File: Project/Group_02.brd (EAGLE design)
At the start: 71.1 x 44.5 mm, 29 parts, among them J1 POWER_JACKPTH_LOCK, U1 +12v

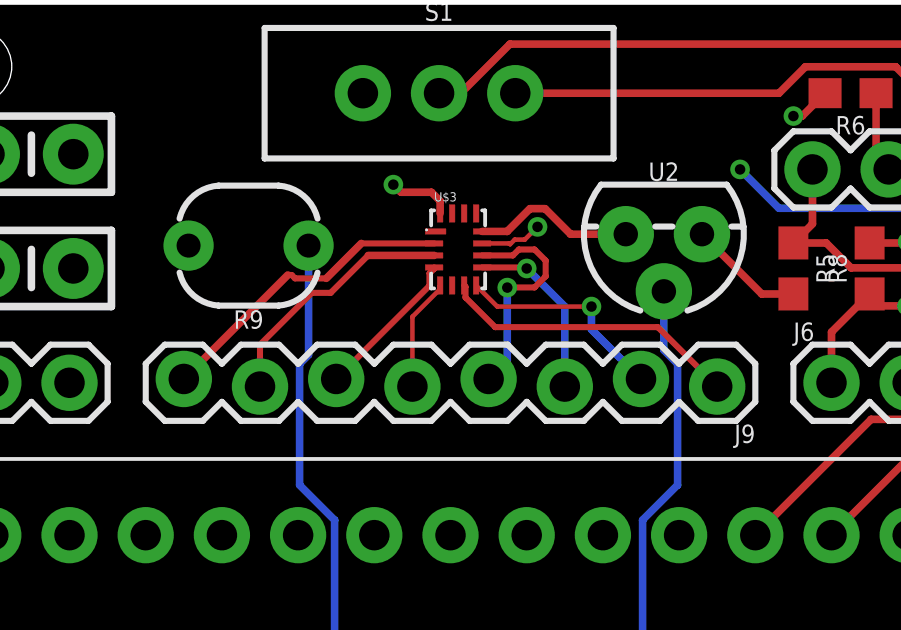
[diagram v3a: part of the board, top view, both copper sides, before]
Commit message: Ancora wire width 10 mils
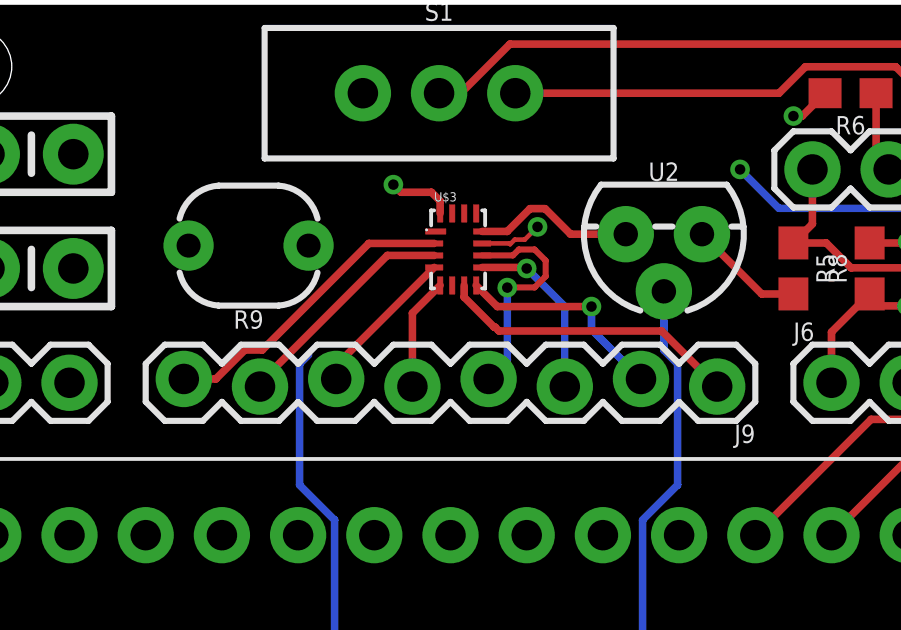
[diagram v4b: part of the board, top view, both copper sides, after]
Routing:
- net PHOTO_OUT: track 38.1 -> 34.5 mm
- net N$11: track 8.43 -> 7.69 mm
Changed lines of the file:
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@@
 <wire x1="24.169" y1="2.54" x2="24.13" y2="2.579" width="0.2032" layer="1"/>
 <wire x1="24.13" y1="2.579" x2="24.13" y2="6.35" width="0.254" layer="1"/>
-<wire x1="14.319" y1="36.322" x2="14.319" y2="32.6802125" width="0.254" layer="16"/>
 <wire x1="14.319" y1="32.6802125" x2="14.0208" y2="32.3820125" width="0.254" layer="16"/>
 <wire x1="15.1874" y1="15.2926" x2="24.13" y2="6.35" width="0.254" layer="16"/>
@@
 <wire x1="14.0208" y1="32.3820125" x2="14.0208" y2="28.34086875" width="0.254" layer="16"/>
 <wire x1="14.0208" y1="28.34086875" x2="15.1874" y2="27.17426875" width="0.254" layer="16"/>
+<wire x1="14.319" y1="32.6802125" x2="14.319" y2="36.322" width="0" layer="19" extent="16-16"/>
 </signal>
 <signal name="TEMP_OUT" class="1">
@@
 <contactref element="U$3" pad="2"/>
 <contactref element="J9" pad="8"/>
-<wire x1="18.504" y1="36.395" x2="16.075" y2="36.395" width="0.2032" layer="1"/>
-<wire x1="13.86659375" y1="35.2298" x2="13.753196875" y2="35.343196875" width="0.2032" layer="1"/>
-<wire x1="13.753196875" y1="35.343196875" x2="13.626196875" y2="35.343196875" width="0.2032" layer="1"/>
-<wire x1="13.626196875" y1="35.343196875" x2="10.16" y2="31.877" width="0.254" layer="1"/>
-<wire x1="16.075" y1="36.395" x2="14.9098" y2="35.2298" width="0.254" layer="1"/>
-<wire x1="14.9098" y1="35.2298" x2="13.86659375" y2="35.2298" width="0.2032" layer="1"/>
+<wire x1="18.504" y1="36.395" x2="16.329" y2="36.395" width="0.254" layer="1"/>
+<wire x1="12.7762" y1="32.8422" x2="12.1949875" y2="32.8422" width="0.254" layer="1"/>
+<wire x1="11.2297875" y1="31.877" x2="10.16" y2="31.877" width="0.254" layer="1"/>
+<wire x1="12.1949875" y1="32.8422" x2="11.2297875" y2="31.877" width="0.254" layer="1"/>
+<wire x1="16.329" y1="36.395" x2="12.7762" y2="32.8422" width="0.254" layer="1"/>
 </signal>
 <signal name="N$11">
 <contactref element="U$3" pad="3"/>
 <contactref element="J9" pad="7"/>
-<wire x1="12.7" y1="31.623" x2="12.7" y2="33.02" width="0.2032" layer="1"/>
-<wire x1="14.4272" y1="34.7472" x2="15.0571" y2="34.7472" width="0.2032" layer="1"/>
-<wire x1="16.3049" y1="35.995" x2="18.504" y2="35.995" width="0.254" layer="1"/>
-<wire x1="15.0571" y1="34.7472" x2="16.3049" y2="35.995" width="0.2032" layer="1"/>
-<wire x1="12.7" y1="33.02" x2="14.4272" y2="34.7472" width="0.2032" layer="1"/>
+<wire x1="18.504" y1="35.995" x2="16.945" y2="35.995" width="0.254" layer="1"/>
+<wire x1="12.7" y1="31.75" x2="12.7" y2="31.623" width="0.254" layer="1"/>
+<wire x1="16.945" y1="35.995" x2="12.7" y2="31.75" width="0.254" layer="1"/>
 </signal>
 <signal name="N$12">
 <contactref element="J9" pad="6"/>
 <contactref element="U$3" pad="4"/>
-<wire x1="15.24" y1="31.877" x2="18.35" y2="34.987" width="0.2032" layer="1"/>
-<wire x1="18.35" y1="34.987" x2="18.35" y2="35.39728125" width="0.2032" layer="1"/>
-<wire x1="18.504" y1="35.55128125" x2="18.504" y2="35.595" width="0.2032" layer="1"/>
-<wire x1="18.35" y1="35.39728125" x2="18.504" y2="35.55128125" width="0.2032" layer="1"/>
+<wire x1="18.504" y1="35.595" x2="15.24" y2="32.331" width="0.254" layer="1"/>
+<wire x1="15.24" y1="32.331" x2="15.24" y2="31.877" width="0.254" layer="1"/>
 </signal>
 <signal name="N$13">
 <contactref element="U$3" pad="5"/>
 <contactref element="J9" pad="5"/>
-<wire x1="17.78" y1="31.623" x2="17.78" y2="33.950025" width="0.1524" layer="1"/>
-<wire x1="17.78" y1="33.950025" x2="18.6802" y2="34.850225" width="0.1524" layer="1"/>
-<wire x1="18.6802" y1="34.850225" x2="18.6802" y2="34.9712" width="0.1524" layer="1"/>
-<wire x1="18.6802" y1="34.9712" x2="18.704" y2="34.995" width="0.1524" layer="1"/>
+<wire x1="18.704" y1="34.995" x2="17.78" y2="34.071" width="0.254" layer="1"/>
+<wire x1="17.78" y1="34.071" x2="17.78" y2="31.623" width="0.254" layer="1"/>
 </signal>
 <signal name="N$14">
@@
 <contactref element="U$3" pad="9"/>
 <contactref element="J9" pad="3"/>
-<wire x1="20.104" y1="35.595" x2="21.555" y2="35.595" width="0.2032" layer="1"/>
-<wire x1="21.555" y1="35.595" x2="21.59" y2="35.56" width="0.2032" layer="1"/>
+<wire x1="20.104" y1="35.595" x2="21.555" y2="35.595" width="0.254" layer="1"/>
+<wire x1="21.555" y1="35.595" x2="21.59" y2="35.56" width="0.254" layer="1"/>
 <via x="21.59" y="35.56" extent="1-16" drill="0.35"/>
 <wire x1="21.59" y1="35.56" x2="22.86" y2="34.29" width="0.254" layer="16"/>
@@
 <wire x1="23.749" y1="33.528" x2="23.749" y2="34.29" width="0.254" layer="16"/>
 <via x="23.749" y="34.29" extent="1-16" drill="0.35"/>
-<wire x1="23.749" y1="34.29" x2="20.609" y2="34.29" width="0.1524" layer="1"/>
-<wire x1="20.609" y1="34.29" x2="19.904" y2="34.995" width="0.1524" layer="1"/>
+<wire x1="20.609" y1="34.29" x2="23.749" y2="34.29" width="0.254" layer="1"/>
+<wire x1="19.904" y1="34.995" x2="20.609" y2="34.29" width="0.254" layer="1"/>
 </signal>
 <signal name="N$17">
 <contactref element="U$3" pad="7"/>
 <contactref element="J9" pad="1"/>
-<wire x1="27.94" y1="31.623" x2="25.9588" y2="33.6042" width="0.2032" layer="1"/>
-<wire x1="19.55" y1="34.59271875" x2="19.55" y2="34.949" width="0.2032" layer="1"/>
-<wire x1="19.55" y1="34.949" x2="19.504" y2="34.995" width="0.2032" layer="1"/>
-<wire x1="25.9588" y1="33.6042" x2="20.53851875" y2="33.6042" width="0.2032" layer="1"/>
-<wire x1="20.53851875" y1="33.6042" x2="19.55" y2="34.59271875" width="0.2032" layer="1"/>
+<wire x1="27.94" y1="31.623" x2="26.0858" y2="33.4772" width="0.254" layer="1"/>
+<wire x1="26.0858" y1="33.4772" x2="20.66551875" y2="33.4772" width="0.254" layer="1"/>
+<wire x1="20.53851875" y1="33.6042" x2="20.66551875" y2="33.4772" width="0.254" layer="1"/>
+<wire x1="20.5026" y1="33.6042" x2="20.53851875" y2="33.6042" width="0.254" layer="1"/>
+<wire x1="19.504" y1="34.995" x2="19.504" y2="34.6028" width="0.254" layer="1"/>
+<wire x1="19.504" y1="34.6028" x2="20.5026" y2="33.6042" width="0.254" layer="1"/>
 </signal>
 <signal name="MUX_OUT/1.4C">

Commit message: Pulizia cavi
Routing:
- net PHOTO_OUT: track 34.5 -> 38.1 mm
- net I2C_A1: track 11.3 -> 10.5 mm
- net I2C_SCL_2: track 11.5 -> 10.7 mm
- net I2C_SCL_1: track 12.0 -> 11.3 mm
- net I2C_SDA_1: track 12.2 -> 11.5 mm
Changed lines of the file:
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@@
 <wire x1="37.74" y1="29.993" x2="37.465" y2="29.718" width="0.254" layer="1"/>
 <via x="37.465" y="29.718" extent="1-16" drill="0.35"/>
-<wire x1="49.149" y1="31.281" x2="48.514" y2="34.5442" width="0" layer="19" extent="1-1"/>
-<wire x1="37.74" y1="30.745" x2="45.72" y2="31.281" width="0" layer="19" extent="1-1"/>
-<wire x1="38.1" y1="36.322" x2="37.74" y2="30.745" width="0" layer="19" extent="1-1"/>
-<wire x1="35.56" y1="36.41" x2="38.1" y2="36.322" width="0" layer="19" extent="1-1"/>
-<wire x1="30.48" y1="34.71" x2="33.02" y2="36.41" width="0" layer="19" extent="1-1"/>
-<wire x1="30.48" y1="40.64" x2="33.02" y2="36.41" width="0" layer="19" extent="1-1"/>
-<wire x1="21.9506" y1="36.9467375" x2="27.432" y2="36.703" width="0" layer="19" extent="1-1"/>
-<wire x1="18.704" y1="37.395" x2="20.104" y2="36.395" width="0" layer="19" extent="1-1"/>
-<wire x1="10.319" y1="36.322" x2="17.145" y2="38.354" width="0" layer="19" extent="1-1"/>
-<wire x1="6.477" y1="35.56" x2="10.319" y2="36.322" width="0" layer="19" extent="1-1"/>
-<wire x1="6.477" y1="39.37" x2="6.477" y2="35.56" width="0" layer="19" extent="1-1"/>
-<wire x1="6.35" y1="31.75" x2="6.477" y2="35.56" width="0" layer="19" extent="1-1"/>
-<wire x1="3.81" y1="26.67" x2="6.35" y2="31.75" width="0" layer="19" extent="1-1"/>
-<wire x1="67.31" y1="6.35" x2="53.975" y2="30.353" width="0" layer="19" extent="1-1"/>
 </signal>
 <signal name="GND">
@@
 <wire x1="21.69925" y1="37.5535375" x2="20.9407125" y2="36.795" width="0.254" layer="1"/>
 <wire x1="20.9407125" y1="36.795" x2="20.104" y2="36.795" width="0.254" layer="1"/>
-<wire x1="62.912" y1="34.1884" x2="58.769" y2="37.9246" width="0" layer="19" extent="1-1"/>
-<wire x1="45.426" y1="39.878" x2="58.769" y2="37.9246" width="0" layer="19" extent="1-1"/>
-<wire x1="43.54" y1="35.295" x2="45.426" y2="39.878" width="0" layer="19" extent="1-1"/>
-<wire x1="43.54" y1="32.045" x2="43.54" y2="35.295" width="0" layer="19" extent="1-1"/>
-<wire x1="38.1" y1="38.851" x2="43.54" y2="35.295" width="0" layer="19" extent="1-1"/>
-<wire x1="24.892" y1="36.703" x2="28.702" y2="38.862" width="0" layer="19" extent="1-1"/>
-<wire x1="3.683" y1="35.56" x2="20.104" y2="36.795" width="0" layer="19" extent="1-1"/>
-<wire x1="3.683" y1="39.37" x2="3.683" y2="35.56" width="0" layer="19" extent="1-1"/>
-<wire x1="3.81" y1="31.75" x2="3.683" y2="35.56" width="0" layer="19" extent="1-1"/>
-<wire x1="6.35" y1="26.67" x2="3.81" y2="31.75" width="0" layer="19" extent="1-1"/>
-<wire x1="19.05" y1="2.54" x2="6.35" y2="26.67" width="0" layer="19" extent="1-1"/>
-<wire x1="25.869" y1="2.54" x2="19.05" y2="2.54" width="0" layer="19" extent="1-1"/>
-<wire x1="64.77" y1="6.35" x2="62.912" y2="34.1884" width="0" layer="19" extent="1-1"/>
 </signal>
 <signal name="12V">
@@
 <wire x1="14.0208" y1="32.3820125" x2="14.0208" y2="28.34086875" width="0.254" layer="16"/>
 <wire x1="14.0208" y1="28.34086875" x2="15.1874" y2="27.17426875" width="0.254" layer="16"/>
-<wire x1="14.319" y1="32.6802125" x2="14.319" y2="36.322" width="0" layer="19" extent="16-16"/>
+<wire x1="14.319" y1="36.322" x2="14.319" y2="32.6802125" width="0.254" layer="16"/>
 </signal>
 <signal name="TEMP_OUT" class="1">
@@
 <contactref element="U$2" pad="10"/>
 <contactref element="R5" pad="1"/>
-<wire x1="37.74" y1="34.645" x2="37.696" y2="34.689" width="0.254" layer="1"/>
-<wire x1="37.696" y1="34.689" x2="37.01838125" y2="34.689" width="0.254" layer="1"/>
 <wire x1="31.115" y1="38.862" x2="31.115" y2="37.045" width="0.254" layer="1"/>
 <wire x1="31.115" y1="37.045" x2="30.48" y2="36.41" width="0.254" layer="1"/>
@@
 <wire x1="45.47386875" y1="34.6938" x2="45.8442" y2="34.32346875" width="0.254" layer="1"/>
 <wire x1="45.8442" y1="34.32346875" x2="45.8442" y2="33.79973125" width="0.254" layer="1"/>
-<wire x1="43.54" y1="33.995" x2="44.25133125" y2="33.995" width="0.254" layer="1"/>
 <wire x1="45.8442" y1="33.79973125" x2="45.7395" y2="33.69503125" width="0.254" layer="1"/>
 <wire x1="45.7395" y1="33.69503125" x2="45.7395" y2="33.0005" width="0.254" layer="1"/>
@@
 <wire x1="51.435" y1="39.243" x2="48.983" y2="36.791" width="0.254" layer="1"/>
 <wire x1="48.983" y1="36.791" x2="48.983" y2="35.56" width="0.254" layer="1"/>
-<wire x1="44.26161875" y1="34.689" x2="43.584" y2="34.689" width="0.254" layer="1"/>
-<wire x1="43.584" y1="34.689" x2="43.54" y2="34.645" width="0.254" layer="1"/>
 <wire x1="48.983" y1="35.56" x2="48.8192125" y2="35.56" width="0.254" layer="1"/>
 <wire x1="48.8192125" y1="35.56" x2="47.9382125" y2="36.441" width="0.254" layer="1"/>
@@
 <contactref element="R2" pad="1"/>
 <wire x1="43.54" y1="32.695" x2="44.45" y2="32.695" width="0.254" layer="1"/>
-<wire x1="44.56086875" y1="32.695" x2="44.5967875" y2="32.695" width="0.254" layer="1"/>
 <wire x1="49.149" y1="32.981" x2="51.015" y2="31.115" width="0.254" layer="1"/>
 <wire x1="51.015" y1="31.115" x2="51.562" y2="31.115" width="0.254" layer="1"/>
@@
 <contactref element="U$1" pad="51"/>
 <contactref element="D1" pad="A"/>
-<wire x1="6.35" y1="6.35" x2="6.35" y2="2.77" width="0.254" layer="1"/>
-<wire x1="6.35" y1="2.77" x2="6.12" y2="2.54" width="0.2032" layer="1"/>
+<wire x1="6.35" y1="2.77" x2="6.35" y2="6.35" width="0.254" layer="1"/>
+<wire x1="6.12" y1="2.54" x2="6.35" y2="2.77" width="0.254" layer="1"/>
 </signal>
 <signal name="N$9">
@@
 <contactref element="U$2" pad="2"/>
 <contactref element="U$1" pad="7"/>
-<wire x1="43.54" y1="31.395" x2="43.584" y2="31.351" width="0.254" layer="1"/>
-<wire x1="43.584" y1="31.351" x2="44.26161875" y2="31.351" width="0.254" layer="1"/>
 <wire x1="49.53" y1="29.21" x2="52.07" y2="26.67" width="0.254" layer="1"/>
-<wire x1="46.3817875" y1="29.21" x2="49.53" y2="29.21" width="0.254" layer="1"/>
-<wire x1="46.3817875" y1="29.23083125" x2="46.3817875" y2="29.21" width="0.254" layer="1"/>
-<wire x1="44.9406" y1="30.61526875" x2="45.10426875" y2="30.4516" width="0.254" layer="1"/>
-<wire x1="45.10426875" y1="30.4516" x2="45.1401875" y2="30.4516" width="0.254" layer="1"/>
-<wire x1="45.1401875" y1="30.4516" x2="46.3817875" y2="29.21" width="0.254" layer="1"/>
-<wire x1="43.54" y1="31.395" x2="44.25354375" y2="31.395" width="0.254" layer="1"/>
-<wire x1="44.25354375" y1="31.395" x2="44.9406" y2="30.70794375" width="0.254" layer="1"/>
-<wire x1="44.9406" y1="30.70794375" x2="44.9406" y2="30.61526875" width="0.254" layer="1"/>
+<wire x1="44.762934375" y1="30.792934375" x2="46.34586875" y2="29.21" width="0.254" layer="1"/>
+<wire x1="46.34586875" y1="29.21" x2="49.53" y2="29.21" width="0.254" layer="1"/>
+<wire x1="44.5694" y1="31.07914375" x2="44.39914375" y2="31.2494" width="0.254" layer="1"/>
+<wire x1="44.39914375" y1="31.2494" x2="43.6856" y2="31.2494" width="0.254" layer="1"/>
+<wire x1="43.6856" y1="31.2494" x2="43.54" y2="31.395" width="0.254" layer="1"/>
+<wire x1="44.762934375" y1="30.792934375" x2="44.5694" y2="30.98646875" width="0.254" layer="1"/>
+<wire x1="44.5694" y1="30.98646875" x2="44.5694" y2="31.07914375" width="0.254" layer="1"/>
 </signal>
 <signal name="I2C_A2">
